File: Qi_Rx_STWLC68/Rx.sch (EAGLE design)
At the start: 44 parts, among them IC1 STWLC68JRH

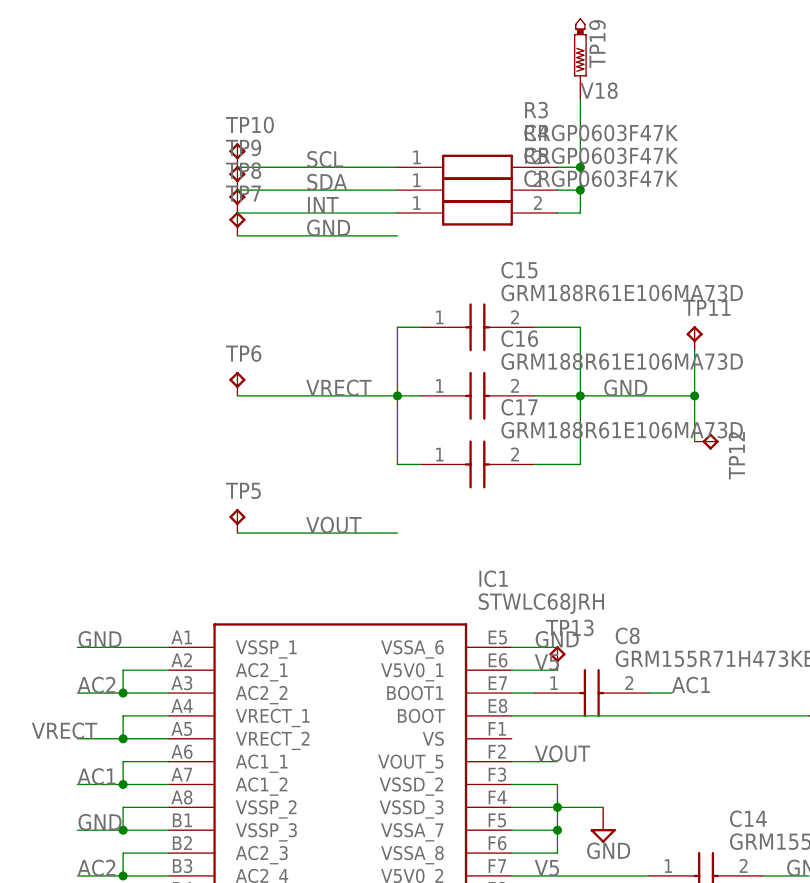
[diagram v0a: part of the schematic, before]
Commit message: Complete SMD layout
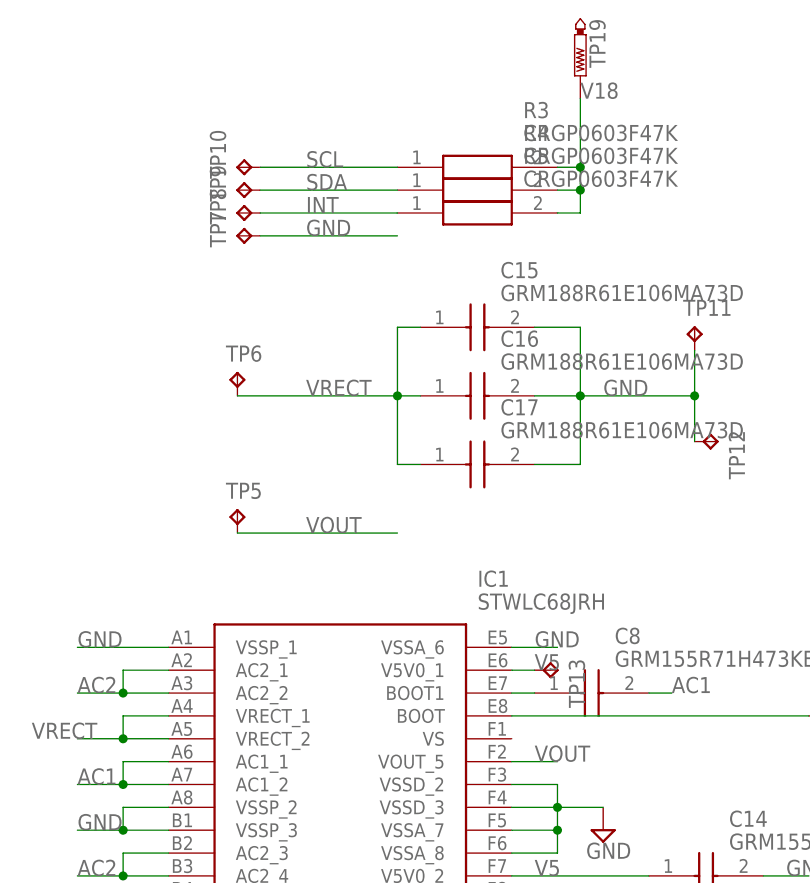
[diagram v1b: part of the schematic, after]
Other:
- moved on the sheet: TP10, TP13, TP7, TP8, TP9
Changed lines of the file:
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@@
 <attribute name="TP_SIGNAL_NAME" x="59.69" y="110.49" size="1.778" layer="97"/>
 </instance>
-<instance part="TP7" gate="G$1" x="58.42" y="129.54" smashed="yes">
-<attribute name="NAME" x="57.15" y="130.81" size="1.778" layer="95"/>
-<attribute name="TP_SIGNAL_NAME" x="59.69" y="128.27" size="1.778" layer="97"/>
-</instance>
-<instance part="TP8" gate="G$1" x="58.42" y="132.08" smashed="yes">
-<attribute name="NAME" x="57.15" y="133.35" size="1.778" layer="95"/>
-<attribute name="TP_SIGNAL_NAME" x="59.69" y="130.81" size="1.778" layer="97"/>
-</instance>
-<instance part="TP9" gate="G$1" x="58.42" y="134.62" smashed="yes">
-<attribute name="NAME" x="57.15" y="135.89" size="1.778" layer="95"/>
-<attribute name="TP_SIGNAL_NAME" x="59.69" y="133.35" size="1.778" layer="97"/>
-</instance>
-<instance part="TP10" gate="G$1" x="58.42" y="137.16" smashed="yes">
-<attribute name="NAME" x="57.15" y="138.43" size="1.778" layer="95"/>
-<attribute name="TP_SIGNAL_NAME" x="59.69" y="135.89" size="1.778" layer="97"/>
+<instance part="TP7" gate="G$1" x="58.42" y="127" smashed="yes" rot="R90">
+<attribute name="NAME" x="57.15" y="125.73" size="1.778" layer="95" rot="R90"/>
+<attribute name="TP_SIGNAL_NAME" x="59.69" y="128.27" size="1.778" layer="97" rot="R90"/>
+</instance>
+<instance part="TP8" gate="G$1" x="58.42" y="129.54" smashed="yes" rot="R90">
+<attribute name="NAME" x="57.15" y="128.27" size="1.778" layer="95" rot="R90"/>
+<attribute name="TP_SIGNAL_NAME" x="59.69" y="130.81" size="1.778" layer="97" rot="R90"/>
+</instance>
+<instance part="TP9" gate="G$1" x="58.42" y="132.08" smashed="yes" rot="R90">
+<attribute name="NAME" x="57.15" y="130.81" size="1.778" layer="95" rot="R90"/>
+<attribute name="TP_SIGNAL_NAME" x="59.69" y="133.35" size="1.778" layer="97" rot="R90"/>
+</instance>
+<instance part="TP10" gate="G$1" x="58.42" y="134.62" smashed="yes" rot="R90">
+<attribute name="NAME" x="57.15" y="133.35" size="1.778" layer="95" rot="R90"/>
+<attribute name="TP_SIGNAL_NAME" x="59.69" y="135.89" size="1.778" layer="97" rot="R90"/>
 </instance>
 <instance part="TP11" gate="G$1" x="109.22" y="116.84" smashed="yes">
@@
 <attribute name="TP_SIGNAL_NAME" x="110.49" y="102.87" size="1.778" layer="97" rot="R270"/>
 </instance>
-<instance part="TP13" gate="G$1" x="93.98" y="81.28" smashed="yes">
-<attribute name="NAME" x="92.71" y="82.55" size="1.778" layer="95"/>
-<attribute name="TP_SIGNAL_NAME" x="95.25" y="80.01" size="1.778" layer="97"/>
+<instance part="TP13" gate="G$1" x="93.98" y="78.74" smashed="yes" rot="R270">
+<attribute name="NAME" x="95.25" y="80.01" size="1.778" layer="95" rot="R270"/>
+<attribute name="TP_SIGNAL_NAME" x="92.71" y="77.47" size="1.778" layer="97" rot="R270"/>
 </instance>
 </instances>
@@
 </segment>
 <segment>
-<wire x1="58.42" y1="127" x2="76.2" y2="127" width="0.1524" layer="91"/>
+<wire x1="60.96" y1="127" x2="76.2" y2="127" width="0.1524" layer="91"/>
 <label x="66.04" y="127" size="1.778" layer="95"/>
 <pinref part="TP7" gate="G$1" pin="TP"/>
@@
 <pinref part="R3" gate="G$1" pin="1"/>
 <label x="66.04" y="134.62" size="1.778" layer="95"/>
-<wire x1="58.42" y1="134.62" x2="76.2" y2="134.62" width="0.1524" layer="91"/>
+<wire x1="60.96" y1="134.62" x2="76.2" y2="134.62" width="0.1524" layer="91"/>
 <pinref part="TP10" gate="G$1" pin="TP"/>
 </segment>
@@
 <pinref part="R4" gate="G$1" pin="1"/>
 <label x="66.04" y="132.08" size="1.778" layer="95"/>
-<wire x1="76.2" y1="132.08" x2="58.42" y2="132.08" width="0.1524" layer="91"/>
+<wire x1="76.2" y1="132.08" x2="60.96" y2="132.08" width="0.1524" layer="91"/>
 <pinref part="TP9" gate="G$1" pin="TP"/>
 </segment>
@@
 <pinref part="R5" gate="G$1" pin="1"/>
 <label x="66.04" y="129.54" size="1.778" layer="95"/>
-<wire x1="76.2" y1="129.54" x2="58.42" y2="129.54" width="0.1524" layer="91"/>
+<wire x1="76.2" y1="129.54" x2="60.96" y2="129.54" width="0.1524" layer="91"/>
 <pinref part="TP8" gate="G$1" pin="TP"/>
 </segment>
@@
 <segment>
 <pinref part="IC1" gate="G$1" pin="V5V0_1"/>
-<wire x1="88.9" y1="78.74" x2="93.98" y2="78.74" width="0.1524" layer="91"/>
+<wire x1="88.9" y1="78.74" x2="91.44" y2="78.74" width="0.1524" layer="91"/>
 <label x="91.44" y="78.74" size="1.778" layer="95"/>
 <pinref part="TP13" gate="G$1" pin="TP"/>

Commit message: Rx surface-mount cleanup
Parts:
- removed TP19: PTR1PAD1-13, testpad:PTR1PAD1-13
- added TP14, TP15: TPPAD1-13, testpad:TPPAD1-13
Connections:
- new net VI2C: R3.2, R4.2, R5.2, TP14.TP
- net GND: now also TP15.TP
- net V18: no longer R3.2, R4.2, R5.2, TP19.TP
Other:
- note added: "1 / 1"
- note added: "<- Coil ->"
- note added: "GPIO Connector"
- note added: "I2C Interface"
- note added: "Power Test Points"
- note added: "Qi Power Module (5W)"
- note added: "Wireless Power"
- moved on the sheet: C1, C10, C11, C12, C13, C14, C15, C16, C17, C18, C19, C2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
